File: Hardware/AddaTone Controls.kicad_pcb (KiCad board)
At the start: 2 copper layers, 60 x 110 mm, 18 parts, among them J1 Conn_01x20_Female, J2 Conn_01x20_Female, J3 PItch_In, J4 Harm1_In, J5 Harm2_In, J6 Freq_Scale_In, J7 DAC1_Out, J8 DAC2_Out, SW1 SW_Push, SW2 SW_Push, SW3 SW_SPST, SW4 SW_SPST

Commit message: Refinements to PCB
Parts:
- J1: value Conn_01x20_Female -> Conn_01x10_Male; footprint Socket_Strips:Socket_Strip_Straight_1x20_Pitch2.54mm -> Pin_Headers:Pin_Header_Straight_1x10_Pitch2.54mm
- J2: value Conn_01x20_Female -> Conn_01x12_Male; footprint Socket_Strips:Socket_Strip_Straight_1x20_Pitch2.54mm -> Pin_Headers:Pin_Header_Straight_1x12_Pitch2.54mm
- moved J1 5.70 mm to (102.8, 102.3)
- moved SW1 2.00 mm to (116.0, 103.5)
- moved SW2 1.50 mm to (150.5, 103.5)
- moved J2 1.20 mm to (155.5, 80.0)
- moved SW3 1.00 mm to (111.5, 87.5)
- moved J8 0.50 mm to (106.0, 151.0)
- moved J5 0.40 mm to (115.6, 151.0)
- moved J6 0.30 mm to (125.2, 151.0)
- moved J4 0.20 mm to (134.8, 151.0)
- moved J3 0.10 mm to (144.4, 151.0)
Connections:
- J1 pad 10: FPGA_DONE -> MIX_SWITCH
- J1 pad 9: FPGA_SI -> RING_MOD
- J2 pad 10: RESET -> +3V3
- J2 pad 11: HARM2_POT -> AUDIO2_OUT
- J2 pad 12: ADC_Data -> AUDIO1_OUT
- J2 pad 4: Net-(J2-Pad4) -> HARM1_CVIN
- J2 pad 5: HARM1_CVIN -> PITCH_CVIN
- J2 pad 6: PITCH_CVIN -> FREQ_SC_POT
- J2 pad 7: FREQ_SC_POT -> Calibration
- J2 pad 8: Net-(J2-Pad8) -> RESET
- J2 pad 9: +3V3 -> HARM2_POT
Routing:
- net +3.3VA: track 0.00 -> 186.9 mm, vias 0 -> 3
- net CV_IN: track 0.00 -> 84.9 mm
- net HARM2_POT: track 0.00 -> 75.0 mm
- net AUDIO2_OUT: track 0.00 -> 72.1 mm
- net HARM1_POT: track 0.00 -> 67.7 mm, vias 0 -> 1
- net HARM1_CVIN: track 0.00 -> 67.0 mm
- net HARM2_CVIN: track 0.00 -> 66.9 mm, vias 0 -> 1
- net PITCH_CVIN: track 0.00 -> 62.4 mm
- net MIX_SWITCH: track 0.00 -> 61.4 mm, vias 0 -> 1
- net FREQ_SCALE_CVIN: track 0.00 -> 50.6 mm, vias 0 -> 1
- net FTUNE: track 0.00 -> 50.4 mm, vias 0 -> 1
- net RESET: track 0.00 -> 49.2 mm
- net RING_MOD: track 0.00 -> 39.2 mm
- net AUDIO1_OUT: track 0.00 -> 38.8 mm
- net HARM_COUNT_POT: track 0.00 -> 38.1 mm
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
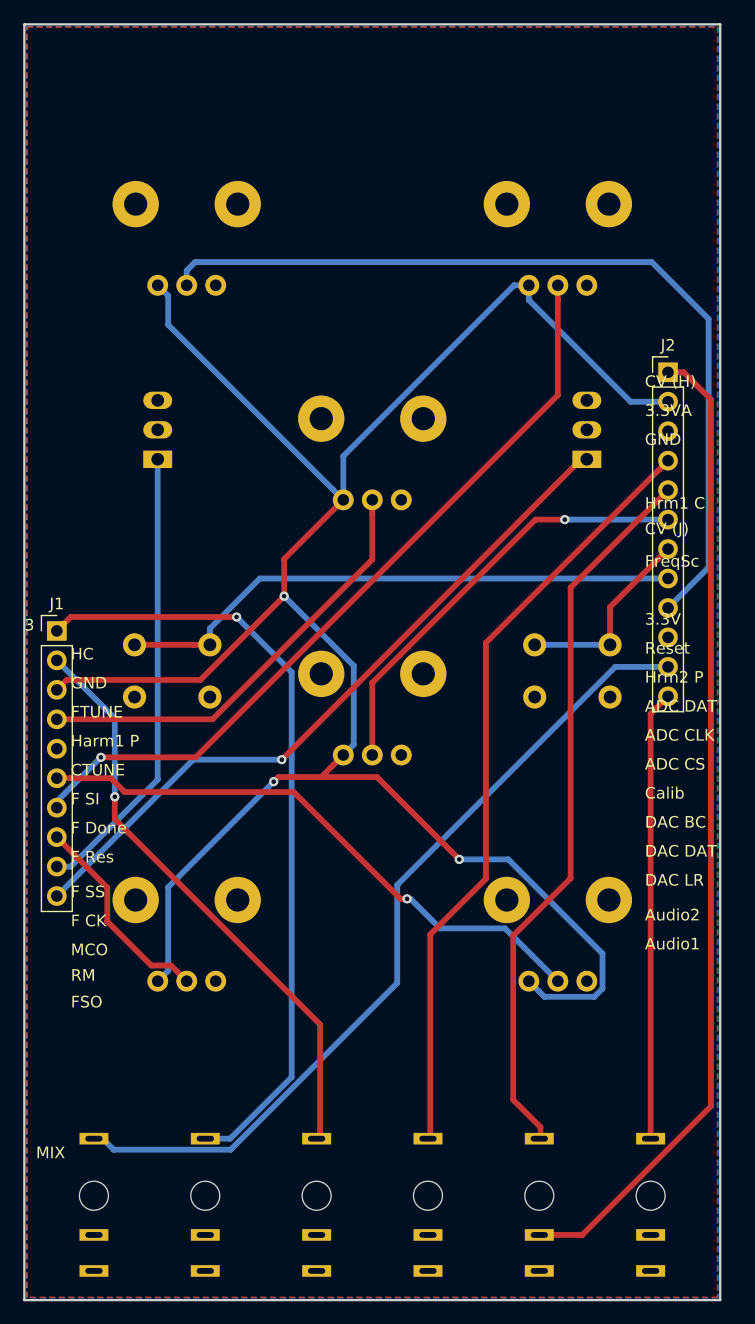
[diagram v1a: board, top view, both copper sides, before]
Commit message: First draft of Panel PCB
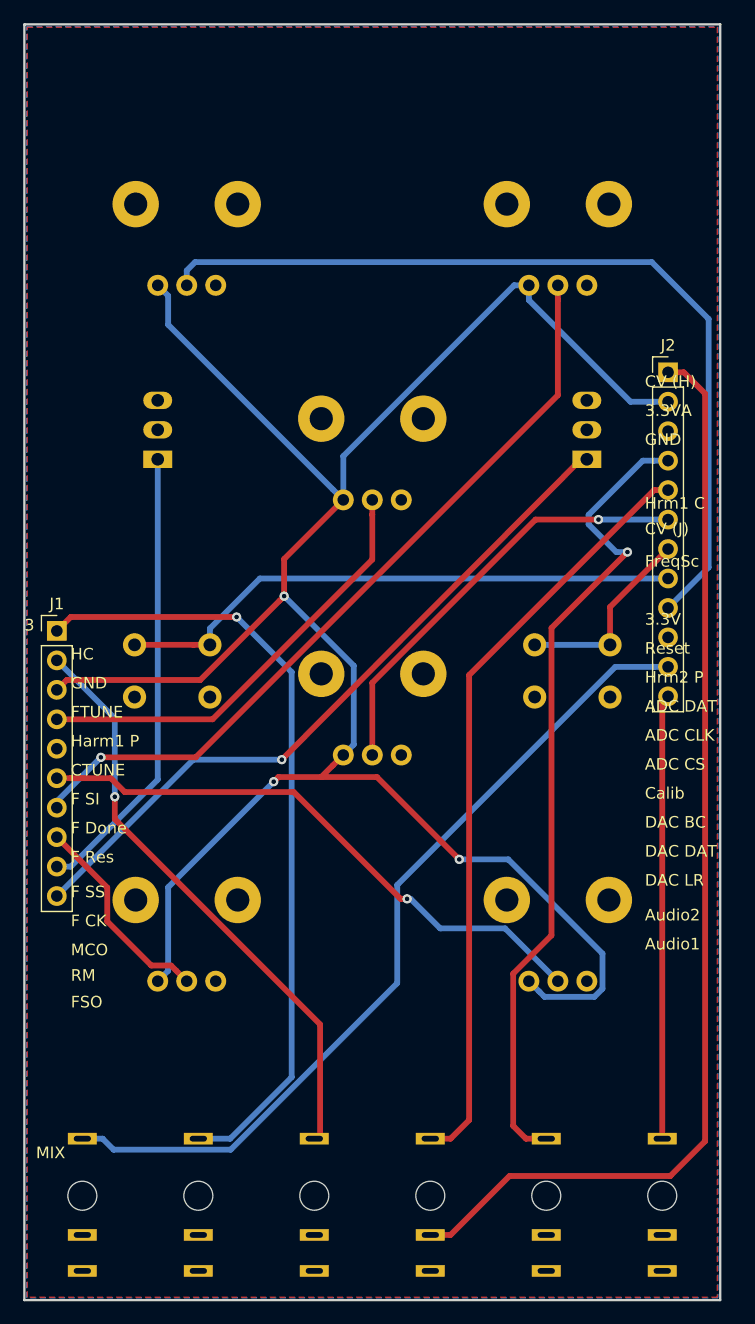
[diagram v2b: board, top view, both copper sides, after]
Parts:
- moved J4 10.2 mm to (145.0, 151.0)
- moved J3 9.40 mm to (135.0, 151.0)
- moved J7 1.00 mm to (155.0, 151.0)
- moved J8 1.00 mm to (105.0, 151.0)
- moved J5 0.60 mm to (115.0, 151.0)
- moved J6 0.20 mm to (125.0, 151.0)
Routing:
- net CV_IN: track 84.9 -> 95.5 mm
- net HARM1_CVIN: track 67.0 -> 70.8 mm, vias 0 -> 1
- net PITCH_CVIN: track 62.4 -> 66.1 mm
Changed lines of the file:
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@@
     (thickness 1.6)
     (drawings 49)
-    (tracks 135)
+    (tracks 144)
     (zones 0)
     (modules 18)
@@
     (solder_mask_min_width 0.25)
     (aux_axis_origin 0 0)
-    (visible_elements 7FFFF77F)
+    (visible_elements 7FFFFF7F)
     (pcbplotparams
       (layerselection 0x010fc_ffffffff)
@@
   )
   (module Custom_Footprints:THONKICONN_hole (layer B.Cu)
-    (at 144.4 151 180)
+    (at 135 151 180)
     (fp_text reference J3 (at 3.81 -6.35) (layer B.SilkS)
       (effects (font (size 1 1) (thickness 0.15)) (justify mirror))
@@
   )
   (module Custom_Footprints:THONKICONN_hole (layer B.Cu)
-    (at 134.8 151 180)
+    (at 145 151 180)
     (fp_text reference J4 (at 3.81 -6.35) (layer B.SilkS)
       (effects (font (size 1 1) (thickness 0.15)) (justify mirror))
@@
   )
   (module Custom_Footprints:THONKICONN_hole (layer B.Cu)
-    (at 115.6 151 180)
+    (at 115 151 180)
     (fp_text reference J5 (at 3.81 -6.35) (layer B.SilkS)
       (effects (font (size 1 1) (thickness 0.15)) (justify mirror))
@@
   )
   (module Custom_Footprints:THONKICONN_hole (layer B.Cu)
-    (at 125.2 151 180)
+    (at 125 151 180)
     (fp_text reference J6 (at 3.81 -6.35) (layer B.SilkS)
       (effects (font (size 1 1) (thickness 0.15)) (justify mirror))
@@
   )
   (module Custom_Footprints:THONKICONN_hole (layer B.Cu)
-    (at 154 151 180)
+    (at 155 151 180)
     (fp_text reference J7 (at 3.81 -6.35) (layer B.SilkS)
       (effects (font (size 1 1) (thickness 0.15)) (justify mirror))
@@
   )
   (module Custom_Footprints:THONKICONN_hole (layer B.Cu)
-    (at 106 151 180)
+    (at 105 151 180)
     (fp_text reference J8 (at 3.81 -6.35) (layer B.SilkS)
       (effects (font (size 1 1) (thickness 0.15)) (justify mirror))
@@
   (segment (start 132.434315 125.4) (end 123.226314 116.191999) (width 0.5) (layer F.Cu) (net 2))
   (segment (start 133 125.4) (end 132.434315 125.4) (width 0.5) (layer F.Cu) (net 2))
-  (segment (start 148.103998 154.38) (end 159.2 143.283998) (width 0.5) (layer F.Cu) (net 3))
-  (segment (start 144.5 154.38) (end 148.103998 154.38) (width 0.5) (layer F.Cu) (net 3))
-  (segment (start 156.85 80) (end 155.5 80) (width 0.5) (layer F.Cu) (net 3))
-  (segment (start 159.2 82.35) (end 156.85 80) (width 0.5) (layer F.Cu) (net 3))
-  (segment (start 159.2 143.283998) (end 159.2 82.35) (width 0.5) (layer F.Cu) (net 3))
+  (segment (start 141.830001 149.299999) (end 136.75 154.38) (width 0.5) (layer F.Cu) (net 3))
+  (segment (start 155.5 80) (end 156.85 80) (width 0.5) (layer F.Cu) (net 3))
+  (segment (start 156.85 80) (end 158.7 81.85) (width 0.5) (layer F.Cu) (net 3))
+  (segment (start 158.7 81.85) (end 158.7 146.3) (width 0.5) (layer F.Cu) (net 3))
+  (segment (start 158.7 146.3) (end 155.700001 149.299999) (width 0.5) (layer F.Cu) (net 3))
+  (segment (start 136.75 154.38) (end 135 154.38) (width 0.5) (layer F.Cu) (net 3))
+  (segment (start 155.700001 149.299999) (end 141.830001 149.299999) (width 0.5) (layer F.Cu) (net 3))
   (segment (start 154.297919 82.54) (end 155.5 82.54) (width 0.5) (layer B.Cu) (net 4))
   (segment (start 152.267208 82.54) (end 154.297919 82.54) (width 0.5) (layer B.Cu) (net 4))
@@
   (segment (start 132.149999 132.669963) (end 132.149999 124.203999) (width 0.5) (layer B.Cu) (net 8))
   (segment (start 106 146.08) (end 106.75 146.08) (width 0.5) (layer B.Cu) (net 8))
-  (segment (start 154 109.44) (end 155.5 107.94) (width 0.5) (layer F.Cu) (net 9))
-  (segment (start 154 146.08) (end 154 109.44) (width 0.5) (layer F.Cu) (net 9))
+  (segment (start 155 108.44) (end 155.5 107.94) (width 0.5) (layer F.Cu) (net 9))
+  (segment (start 155 146.08) (end 155 108.44) (width 0.5) (layer F.Cu) (net 9))
   (segment (start 148.5 87.5) (end 148 87.5) (width 0.5) (layer F.Cu) (net 10))
   (via (at 122.2 113.4) (size 0.8) (drill 0.4) (layers F.Cu B.Cu) (net 10))
@@
   (segment (start 114.773998 113.2) (end 146 81.973998) (width 0.5) (layer F.Cu) (net 13))
   (segment (start 106.6 113.2) (end 114.773998 113.2) (width 0.5) (layer F.Cu) (net 13))
-  (segment (start 144.073998 92.7) (end 146.6 92.7) (width 0.5) (layer F.Cu) (net 14))
-  (via (at 146.6 92.7) (size 0.8) (drill 0.4) (layers F.Cu B.Cu) (net 14))
-  (segment (start 130 113) (end 130 106.773998) (width 0.5) (layer F.Cu) (net 14))
-  (segment (start 130 106.773998) (end 144.073998 92.7) (width 0.5) (layer F.Cu) (net 14))
-  (segment (start 147.165685 92.7) (end 155.5 92.7) (width 0.5) (layer B.Cu) (net 14))
-  (segment (start 146.6 92.7) (end 147.165685 92.7) (width 0.5) (layer B.Cu) (net 14))
+  (segment (start 149.5 92.7) (end 144.073998 92.7) (width 0.5) (layer F.Cu) (net 14))
+  (segment (start 130 106.773998) (end 130 113) (width 0.5) (layer F.Cu) (net 14))
+  (via (at 149.5 92.7) (size 0.8) (drill 0.4) (layers F.Cu B.Cu) (net 14))
+  (segment (start 144.073998 92.7) (end 130 106.773998) (width 0.5) (layer F.Cu) (net 14))
+  (segment (start 149.5 92.7) (end 155.5 92.7) (width 0.5) (layer B.Cu) (net 14))
   (segment (start 107.8 118.526002) (end 107.8 116.6) (width 0.5) (layer F.Cu) (net 15))
   (segment (start 125.5 146.08) (end 125.5 136.226002) (width 0.5) (layer F.Cu) (net 15))
@@
   (segment (start 104 101.1) (end 102.8 102.3) (width 0.5) (layer F.Cu) (net 16))
   (segment (start 118.3 101.1) (end 104 101.1) (width 0.5) (layer F.Cu) (net 16))
-  (segment (start 135 128.473998) (end 139.8 123.673998) (width 0.5) (layer F.Cu) (net 17))
-  (segment (start 135 146.08) (end 135 128.473998) (width 0.5) (layer F.Cu) (net 17))
-  (segment (start 139.8 103.32) (end 155.5 87.62) (width 0.5) (layer F.Cu) (net 17))
-  (segment (start 139.8 123.673998) (end 139.8 103.32) (width 0.5) (layer F.Cu) (net 17))
-  (segment (start 142.149999 128.576003) (end 147.1 123.626002) (width 0.5) (layer F.Cu) (net 18))
-  (segment (start 142.149999 142.729999) (end 142.149999 128.576003) (width 0.5) (layer F.Cu) (net 18))
-  (segment (start 144.5 146.08) (end 144.5 145.08) (width 0.5) (layer F.Cu) (net 18))
-  (segment (start 144.5 145.08) (end 142.149999 142.729999) (width 0.5) (layer F.Cu) (net 18))
-  (segment (start 147.1 98.56) (end 155.5 90.16) (width 0.5) (layer F.Cu) (net 18))
-  (segment (start 147.1 123.626002) (end 147.1 98.56) (width 0.5) (layer F.Cu) (net 18))
+  (via (at 152 95.5) (size 0.8) (drill 0.4) (layers F.Cu B.Cu) (net 17))
+  (segment (start 143.25 146.08) (end 142.149999 144.979999) (width 0.5) (layer F.Cu) (net 17))
+  (segment (start 145 146.08) (end 143.25 146.08) (width 0.5) (layer F.Cu) (net 17))
+  (segment (start 145.450001 102.049999) (end 152 95.5) (width 0.5) (layer F.Cu) (net 17))
+  (segment (start 142.149999 144.979999) (end 142.149999 131.851999) (width 0.5) (layer F.Cu) (net 17))
+  (segment (start 142.149999 131.851999) (end 145.450001 128.551997) (width 0.5) (layer F.Cu) (net 17))
+  (segment (start 145.450001 128.551997) (end 145.450001 102.049999) (width 0.5) (layer F.Cu) (net 17))
+  (segment (start 154.297919 87.62) (end 155.5 87.62) (width 0.5) (layer B.Cu) (net 17))
+  (segment (start 153.321998 87.62) (end 154.297919 87.62) (width 0.5) (layer B.Cu) (net 17))
+  (segment (start 148.649999 92.291999) (end 153.321998 87.62) (width 0.5) (layer B.Cu) (net 17))
+  (segment (start 151.041998 95.5) (end 148.649999 93.108001) (width 0.5) (layer B.Cu) (net 17))
+  (segment (start 148.649999 93.108001) (end 148.649999 92.291999) (width 0.5) (layer B.Cu) (net 17))
+  (segment (start 152 95.5) (end 151.041998 95.5) (width 0.5) (layer B.Cu) (net 17))
+  (segment (start 154.297919 90.16) (end 155.5 90.16) (width 0.5) (layer F.Cu) (net 18))
+  (segment (start 138.350001 106.107918) (end 154.297919 90.16) (width 0.5) (layer F.Cu) (net 18))
+  (segment (start 138.350001 144.479999) (end 138.350001 106.107918) (width 0.5) (layer F.Cu) (net 18))
+  (segment (start 136.75 146.08) (end 138.350001 144.479999) (width 0.5) (layer F.Cu) (net 18))
+  (segment (start 135 146.08) (end 136.75 146.08) (width 0.5) (layer F.Cu) (net 18))
   (segment (start 130 96.146002) (end 130 92.272792) (width 0.5) (layer F.Cu) (net 19))
   (segment (start 130 92.272792) (end 130 91) (width 0.5) (layer F.Cu) (net 19))

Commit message: Further updates to PCBs
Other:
- board text added: "3V3A"
- board text added: "Audio 1"
- board text added: "Audio 2"
- board text added: "E"
- board text added: "FS Pot"
- board text added: "FSCV"
- board text added: "H1CV"
- board text added: "H2CV"
- board text added: "Harm 1"
- board text added: "Harm 2"
- board text added: "Harm Cnt"
- board text added: "Harm1 Pot"
- board text added: "Harm2 Pot"
- board text added: "Mix"
- board text added: "O"
- board text added: "Pitch"
- board text added: "Ring Mod"
- board text added: "Warp"
- board text removed: "3"
- board text removed: "3.3VA"
- board text removed: "ADC CLK"
- board text removed: "ADC CS"
- board text removed: "ADC DAT"
- board text removed: "Audio1"
- board text removed: "Audio2"
- board text removed: "DAC BC"
- board text removed: "DAC DAT"
- board text removed: "DAC LR"
- board text removed: "F CK"
- board text removed: "F Done"
- board text removed: "F Res"
- board text removed: "F SI"
- board text removed: "F SS"
- board text removed: "FSO"
- board text removed: "FreqSc"
- board text removed: "HC"
- board text removed: "Harm1 P"
- board text removed: "Hrm1 C"
- board text removed: "Hrm2 P"
- board text removed: "MCO"

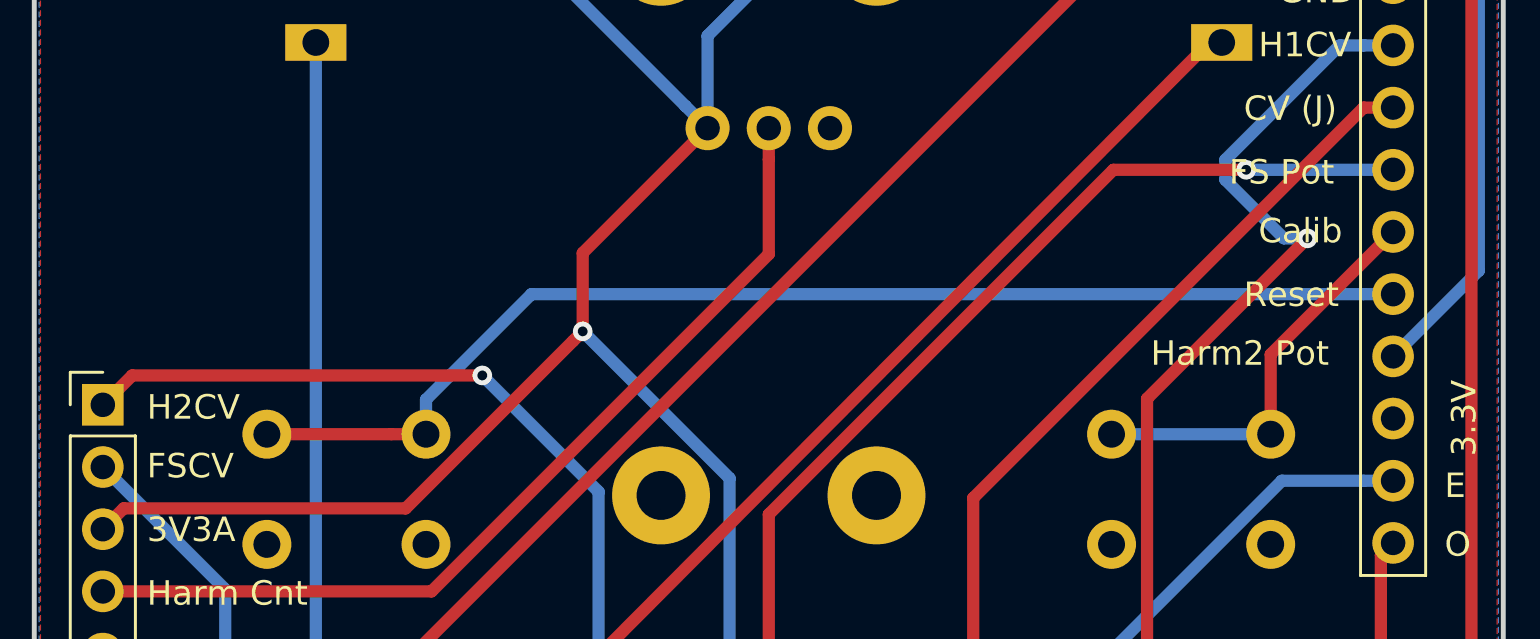
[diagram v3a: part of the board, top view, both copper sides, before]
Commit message: Updated FPGA programming code to use correct pin for Reset; Minor PCB corrections
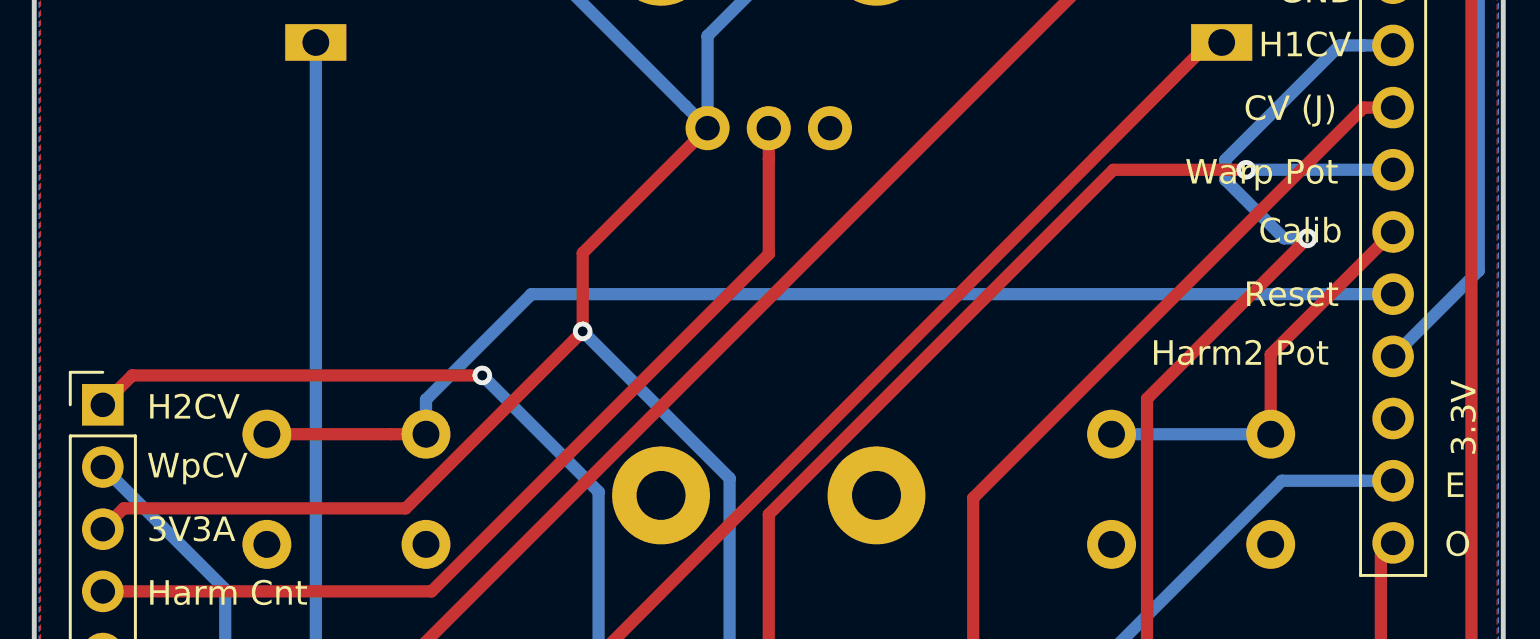
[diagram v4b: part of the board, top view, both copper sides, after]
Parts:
- J3: value PItch_In -> Pitch_In
- J6: value Freq_Scale_In -> Warp_In
- renumbered FreqScale1 to Warp1
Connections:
- net FREQ_SCALE_CVIN renamed WARP_CVIN
- net FREQ_SC_POT renamed WARP_POT
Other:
- board text added: "Warp Pot"
- board text added: "WpCV"
- board text removed: "FS Pot"
- board text removed: "FSCV"
